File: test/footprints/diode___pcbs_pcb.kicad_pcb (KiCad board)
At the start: 2 copper layers, 1 part

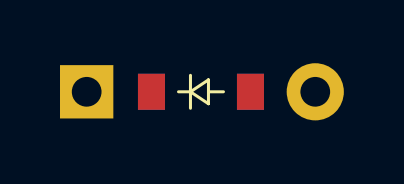
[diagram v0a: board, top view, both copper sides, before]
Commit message: TEST: Fix tests for new power netclass
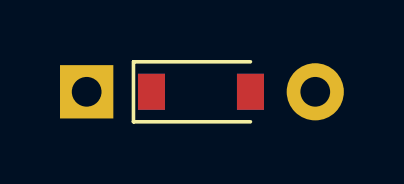
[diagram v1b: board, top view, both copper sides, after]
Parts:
- D1: value (none) -> D_SOD-123; footprint ComboDiode -> Diode_SMD:D_SOD-123
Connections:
- D1 pad 1: to -> from
- D1 pad 2: from -> to
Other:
- net class Power added: clearance 0.2, trace_width 0.5, via_dia 0.8, via_drill 0.4
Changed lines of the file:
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@@
 (add_net "to")
   )
-    (module ComboDiode (layer F.Cu)
-        (at 0 0 0)
-        (fp_text reference "D1" (at 0 0) (layer F.SilkS) hide (effects (font (size 1.27 1.27) (thickness 0.15))))
-        (fp_text value "" (at 0 0) (layer F.SilkS) hide (effects (font (size 1.27 1.27) (thickness 0.15))))
-        (fp_line (start 0.25 0) (end 0.75 0) (layer F.SilkS) (width 0.1))
-        (fp_line (start 0.25 0.4) (end -0.35 0) (layer F.SilkS) (width 0.1))
-        (fp_line (start 0.25 -0.4) (end 0.25 0.4) (layer F.SilkS) (width 0.1))
-        (fp_line (start -0.35 0) (end 0.25 -0.4) (layer F.SilkS) (width 0.1))
-        (fp_line (start -0.35 0) (end -0.35 0.55) (layer F.SilkS) (width 0.1))
-        (fp_line (start -0.35 0) (end -0.35 -0.55) (layer F.SilkS) (width 0.1))
-        (fp_line (start -0.75 0) (end -0.35 0) (layer F.SilkS) (width 0.1))
-        (fp_line (start 0.25 0) (end 0.75 0) (layer B.SilkS) (width 0.1))
-        (fp_line (start 0.25 0.4) (end -0.35 0) (layer B.SilkS) (width 0.1))
-        (fp_line (start 0.25 -0.4) (end 0.25 0.4) (layer B.SilkS) (width 0.1))
-        (fp_line (start -0.35 0) (end 0.25 -0.4) (layer B.SilkS) (width 0.1))
-        (fp_line (start -0.35 0) (end -0.35 0.55) (layer B.SilkS) (width 0.1))
-        (fp_line (start -0.35 0) (end -0.35 -0.55) (layer B.SilkS) (width 0.1))
-        (fp_line (start -0.75 0) (end -0.35 0) (layer B.SilkS) (width 0.1))
-        (pad 1 smd rect (at -1.65 0 0) (size 0.9 1.2) (layers F.Cu F.Paste F.Mask) (net 2 "to"))
-        (pad 2 smd rect (at 1.65 0 0) (size 0.9 1.2) (layers B.Cu B.Paste B.Mask) (net 1 "from"))
-        (pad 1 smd rect (at -1.65 0 0) (size 0.9 1.2) (layers B.Cu B.Paste B.Mask) (net 2 "to"))
-        (pad 2 smd rect (at 1.65 0 0) (size 0.9 1.2) (layers F.Cu F.Paste F.Mask) (net 1 "from"))
-        (pad 1 thru_hole rect (at -3.81 0 0) (size 1.778 1.778) (drill 0.9906) (layers *.Cu *.Mask) (net 2 "to"))
-        (pad 2 thru_hole circle (at 3.81 0 0) (size 1.905 1.905) (drill 0.9906) (layers *.Cu *.Mask) (net 1 "from"))
-    )
+  (net_class Power "This is the power net class."
+    (clearance 0.2)
+    (trace_width 0.5)
+    (via_dia 0.8)
+    (via_drill 0.4)
+    (uvia_dia 0.3)
+    (uvia_drill 0.1)
+  )
+            (footprint "Diode_SMD:D_SOD-123" (layer "F.Cu")
+            (at 0 0 0)
+            (descr "SOD-123")
+            (tags "SOD-123")
+            (attr smd)
+            (fp_text reference "D1" (at 0 -2) (layer "F.SilkS") hide (effects (font (size 1 1) (thickness 0.15))))
+            (fp_text value "D_SOD-123" (at 0 2.1) (layer "F.Fab") (effects (font (size 1 1) (thickness 0.15))))
+            (fp_text user "D1" (at 0 -2) (layer "F.Fab") (effects (font (size 1 1) (thickness 0.15))))
+            (fp_line (start -2.25 1) (end 1.65 1) (layer "F.SilkS") (width 0.12))
+            (fp_line (start -2.25 -1) (end -2.25 1) (layer "F.SilkS") (width 0.12))
+            (fp_line (start -2.25 -1) (end 1.65 -1) (layer "F.SilkS") (width 0.12))
+            (fp_line (start -2.35 -1.15) (end -2.35 1.15) (layer "F.CrtYd") (width 0.05))
+            (fp_line (start 2.35 1.15) (end -2.35 1.15) (layer "F.CrtYd") (width 0.05))
+            (fp_line (start -2.35 -1.15) (end 2.35 -1.15) (layer "F.CrtYd") (width 0.05))
+            (fp_line (start 2.35 -1.15) (end 2.35 1.15) (layer "F.CrtYd") (width 0.05))
+            (fp_line (start 0.25 0) (end 0.75 0) (layer "F.Fab") (width 0.1))
+            (fp_line (start -0.35 0) (end 0.25 -0.4) (layer "F.Fab") (width 0.1))
+            (fp_line (start -0.35 0) (end -0.35 0.55) (layer "F.Fab") (width 0.1))
+            (fp_line (start -0.35 0) (end -0.35 -0.55) (layer "F.Fab") (width 0.1))
+            (fp_line (start 0.25 -0.4) (end 0.25 0.4) (layer "F.Fab") (width 0.1))
+            (fp_line (start 1.4 -0.9) (end 1.4 0.9) (layer "F.Fab") (width 0.1))
+            (fp_line (start 1.4 0.9) (end -1.4 0.9) (layer "F.Fab") (width 0.1))
+            (fp_line (start -0.75 0) (end -0.35 0) (layer "F.Fab") (width 0.1))
+            (fp_line (start -1.4 0.9) (end -1.4 -0.9) (layer "F.Fab") (width 0.1))
+            (fp_line (start 0.25 0.4) (end -0.35 0) (layer "F.Fab") (width 0.1))
+            (fp_line (start -1.4 -0.9) (end 1.4 -0.9) (layer "F.Fab") (width 0.1))
+                (pad "1" smd rect (at -1.65 0 0) (size 0.9 1.2) (layers "F.Cu" "F.Paste" "F.Mask") (net 2 "to"))
+                (pad "2" smd rect (at 1.65 0 0) (size 0.9 1.2) (layers "B.Cu" "B.Paste" "B.Mask") (net 1 "from"))
+                (pad "1" smd rect (at -1.65 0 0) (size 0.9 1.2) (layers "B.Cu" "B.Paste" "B.Mask") (net 2 "to"))
+                (pad "2" smd rect (at 1.65 0 0) (size 0.9 1.2) (layers "F.Cu" "F.Paste" "F.Mask") (net 1 "from"))
+                (pad 1 thru_hole circle (at 3.81 0 0) (size 1.905 1.905) (drill 0.9906) (layers *.Cu *.Mask) (net 1 "from"))
+                (pad 2 thru_hole rect (at -3.81 0 0) (size 1.778 1.778) (drill 0.9906) (layers *.Cu *.Mask) (net 2 "to"))
+            (model "${KICAD6_3DMODEL_DIR}/Diode_SMD.3dshapes/D_SOD-123.wrl"
+                (offset (xyz 0 0 0))
+                (scale (xyz 1 1 1))
+                (rotate (xyz 0 0 0))
+            )
+            )
 )
